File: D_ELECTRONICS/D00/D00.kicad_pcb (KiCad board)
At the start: 2 copper layers, 58.4 x 27.9 mm, 15 parts, among them J0 Conn_01x01_Male, J1 Conn_01x01_Male, J2 Conn_01x01_Male, J3 Conn_01x01_Male, J4 Conn_01x02_Female, J5 Conn_01x04_Female

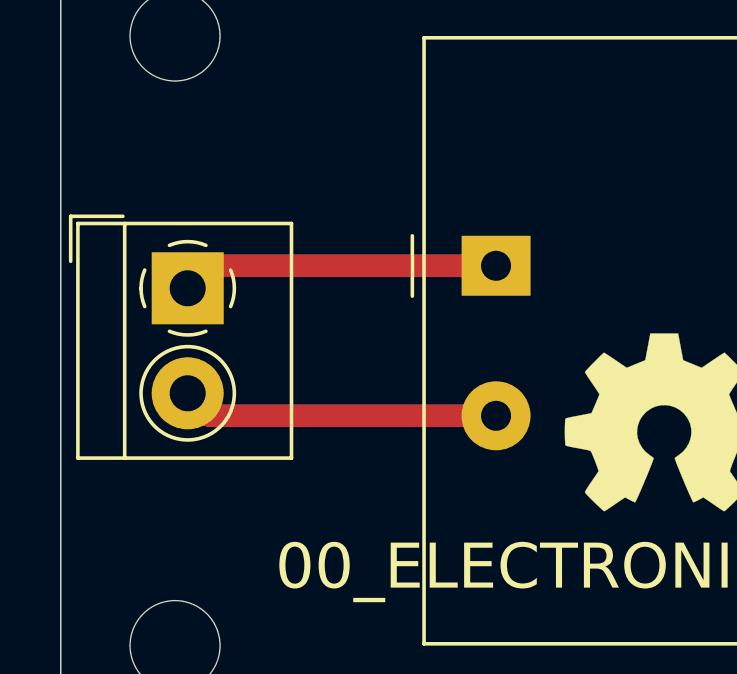
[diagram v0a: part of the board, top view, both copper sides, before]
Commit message: bigger screw terminal for the AC side
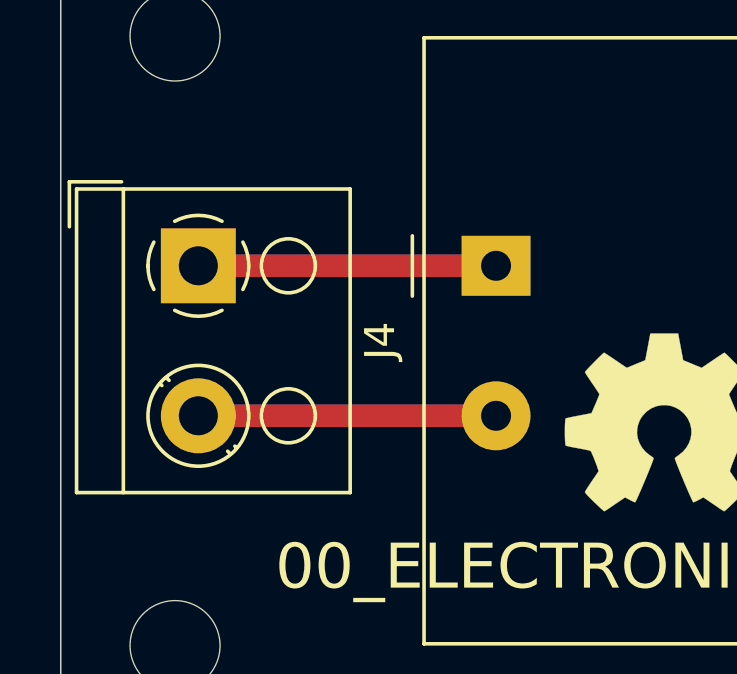
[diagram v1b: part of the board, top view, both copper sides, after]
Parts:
- J4: footprint TerminalBlock_4Ucon:TerminalBlock_4Ucon_1x02_P3.50mm_Horizontal -> TerminalBlock_RND:TerminalBlock_RND_205-00001_1x02_P5.00mm_Horizontal
- moved J4 0.83 mm to (24.6, 31.5)
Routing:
- net Net-(J4-Pad2): track 21.2 -> 19.8 mm
- net Net-(J4-Pad1): track 21.2 -> 19.8 mm

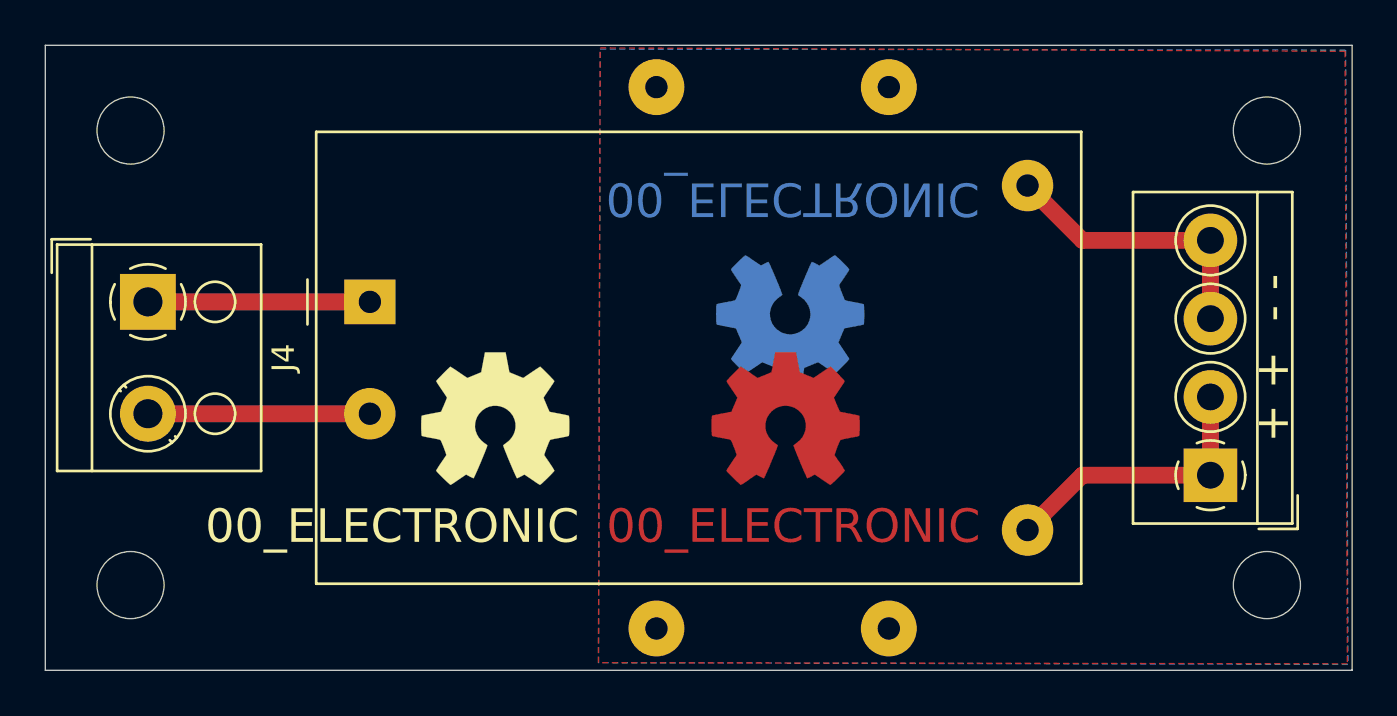
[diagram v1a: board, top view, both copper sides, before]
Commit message: fixed silkscreen part number
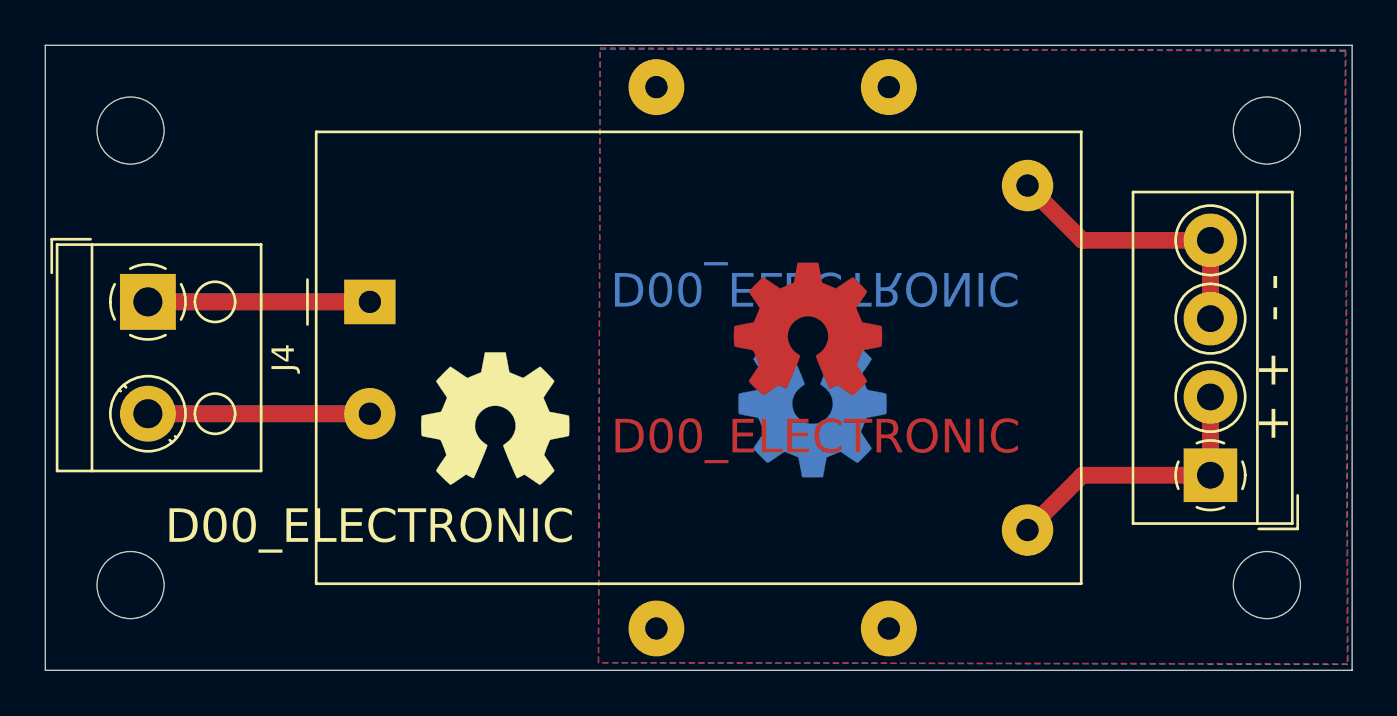
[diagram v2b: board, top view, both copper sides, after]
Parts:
- moved REF** 4.12 mm to (54.1, 32.7)
- moved REF** 4.12 mm to (54.3, 36.3)
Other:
- board text added: "D00_ELECTRONIC"
- board text removed: "00_ELECTRONIC"
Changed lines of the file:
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@@
   )
   (module Symbol:OSHW-Symbol_6.7x6mm_Copper (layer F.Cu)
-    (at 53.086 36.703)
+    (at 54.086 32.703)
     (descr "Open Source Hardware Symbol")
     (tags "Logo Symbol OSHW")
@@
   )
   (module Symbol:OSHW-Symbol_6.7x6mm_Copper (layer B.Cu)
-    (at 53.2892 32.3342)
+    (at 54.2892 36.3342)
     (descr "Open Source Hardware Symbol")
     (tags "Logo Symbol OSHW")
@@
     (effects (font (size 1.5 1.5) (thickness 0.15)))
   )
-  (gr_text 00_ELECTRONIC (at 53.4162 26.8732 180) (layer B.Cu)
+  (gr_text D00_ELECTRONIC (at 54.4162 30.8732 180) (layer B.Cu)
     (effects (font (size 1.5 1.5) (thickness 0.3)) (justify mirror))
   )
-  (gr_text 00_ELECTRONIC (at 53.4416 41.5036) (layer F.Cu)
+  (gr_text D00_ELECTRONIC (at 54.4416 37.5036) (layer F.Cu)
     (effects (font (size 1.5 1.5) (thickness 0.3)))
   )
-  (gr_text 00_ELECTRONIC (at 35.5092 26.8732 180) (layer B.SilkS)
+  (gr_text D00_ELECTRONIC (at 34.5 26.8732 180) (layer B.SilkS)
     (effects (font (size 1.5 1.5) (thickness 0.15)) (justify mirror))
   )
-  (gr_text 00_ELECTRONIC (at 35.5092 41.5036) (layer F.SilkS)
+  (gr_text D00_ELECTRONIC (at 34.5 41.5036) (layer F.SilkS)
     (effects (font (size 1.5 1.5) (thickness 0.15)))
   )
